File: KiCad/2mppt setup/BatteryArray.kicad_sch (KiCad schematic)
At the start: 4 parts

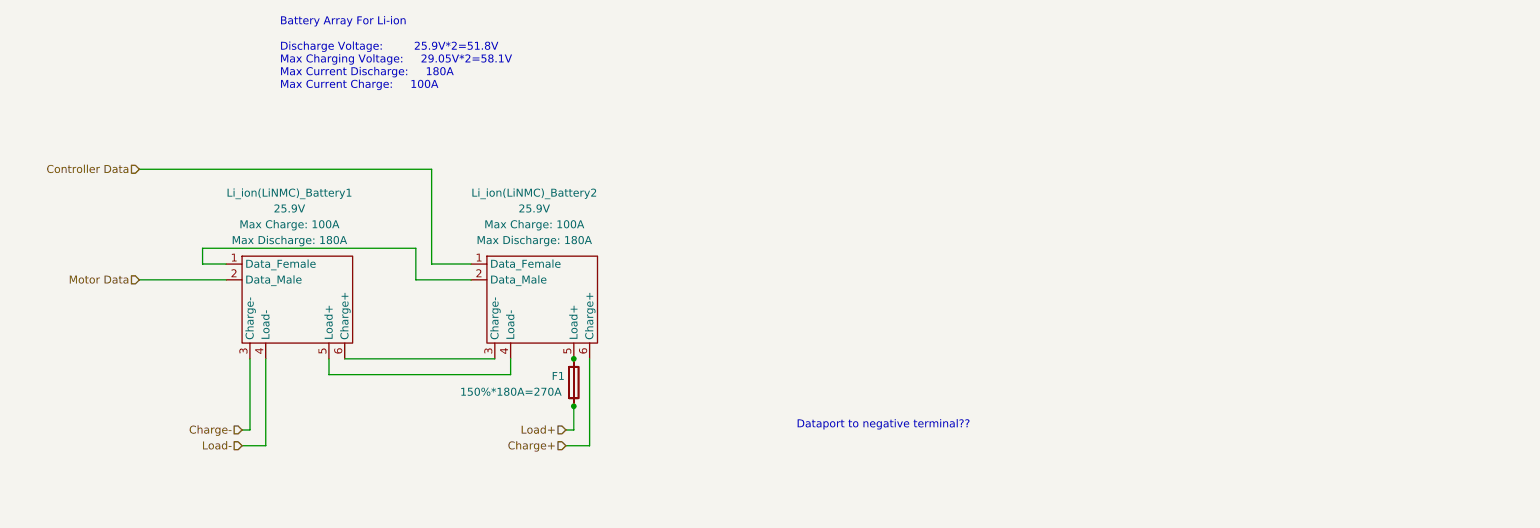
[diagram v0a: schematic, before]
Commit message: Fix wiring check issue
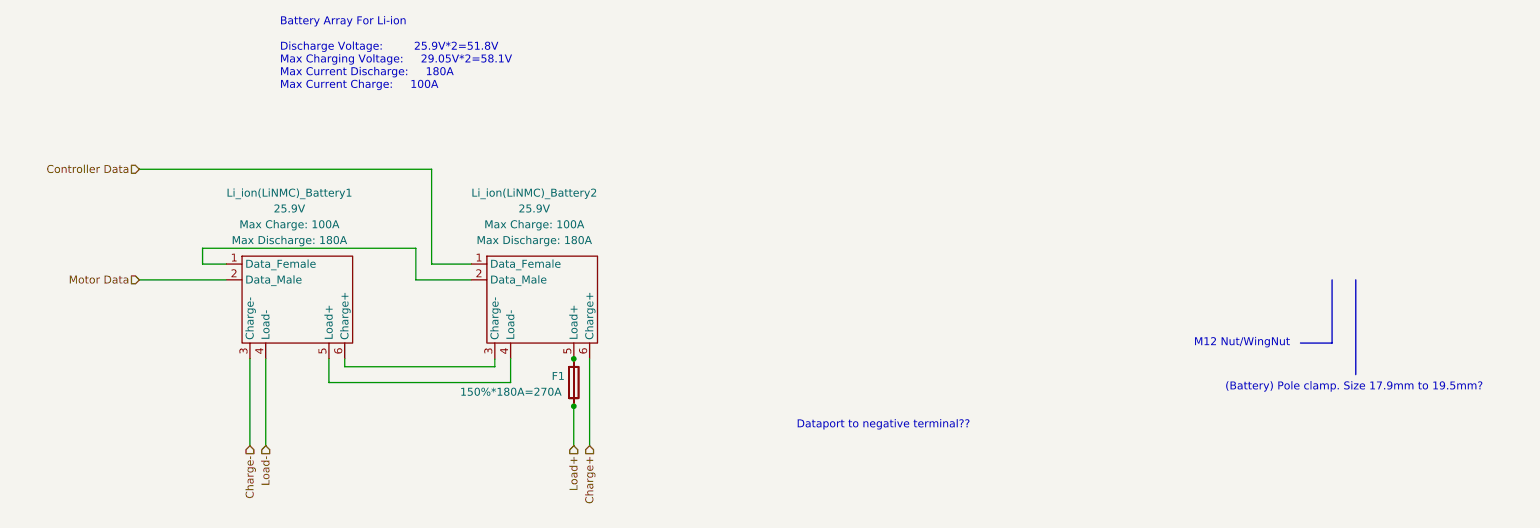
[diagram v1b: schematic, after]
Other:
- note added: "(Battery) Pole clamp. Size 17.9mm to 19.5mm?"
- note added: "M12 Nut/WingNut"

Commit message: KiCad_Skip & Schemdraw test
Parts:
- renumbered 150%*180A=270A_1 to 150%*180A=270A_2, F1 to F2, Li_ion(LiNMC)_Battery1 to Li_ion(LiNMC)_Battery3, Li_ion(LiNMC)_Battery2 to Li_ion(LiNMC)_Battery4
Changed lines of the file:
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@@
 	(text "Battery Array For Li-ion\n\nDischarge Voltage:	 	25.9V*2=51.8V\nMax Charging Voltage: 	29.05V*2=58.1V \nMax Current Discharge: 	180A\nMax Current Charge: 	100A"
 		(exclude_from_sim yes)
-		(at 86.106 25.908 0)
+		(at 85.852 34.29 0)
 		(effects
 			(font
@@
 		(dnp no)
 		(fields_autoplaced yes)
-		(property "Reference" "Li_ion(LiNMC)_Battery2"
+		(property "Reference" "Li_ion(LiNMC)_Battery4"
 			(at 127 48.26 0)
 			(effects
@@
 		(instances
 			(project "2mppt setup"
+				(path "/a5748c52-e651-4363-96d3-c9fc6357a5ef/3557b8e6-13fd-4121-8a05-5ebfb3204dff"
+					(reference "Li_ion(LiNMC)_Battery4")
+					(unit 1)
+				)
 				(path "/a5748c52-e651-4363-96d3-c9fc6357a5ef/5c90004e-845d-4999-8ab5-0ca9dd600da9"
 					(reference "Li_ion(LiNMC)_Battery2")
@@
 		(on_board yes)
 		(dnp no)
-		(property "Reference" "150%*180A=270A_1"
+		(property "Reference" "150%*180A=270A_2"
 			(at 113.538 79.502 0)
 			(effects
@@
 		)
 		(instances
-			(project ""
+			(project "2mppt setup"
+				(path "/a5748c52-e651-4363-96d3-c9fc6357a5ef/3557b8e6-13fd-4121-8a05-5ebfb3204dff"
+					(reference "150%*180A=270A_2")
+					(unit 1)
+				)
 				(path "/a5748c52-e651-4363-96d3-c9fc6357a5ef/5c90004e-845d-4999-8ab5-0ca9dd600da9"
 					(reference "150%*180A=270A_1")
@@
 		(dnp no)
 		(fields_autoplaced yes)
-		(property "Reference" "Li_ion(LiNMC)_Battery1"
+		(property "Reference" "Li_ion(LiNMC)_Battery3"
 			(at 87.63 48.26 0)
 			(effects
@@
 		)
 		(instances
-			(project ""
+			(project "2mppt setup"
+				(path "/a5748c52-e651-4363-96d3-c9fc6357a5ef/3557b8e6-13fd-4121-8a05-5ebfb3204dff"
+					(reference "Li_ion(LiNMC)_Battery3")
+					(unit 1)
+				)
 				(path "/a5748c52-e651-4363-96d3-c9fc6357a5ef/5c90004e-845d-4999-8ab5-0ca9dd600da9"
 					(reference "Li_ion(LiNMC)_Battery1")
@@
 		(on_board yes)
 		(dnp no)
-		(property "Reference" "F1"
+		(property "Reference" "F2"
 			(at 129.794 77.724 0)
 			(effects
@@
 		)
 		(instances
-			(project ""
+			(project "2mppt setup"
+				(path "/a5748c52-e651-4363-96d3-c9fc6357a5ef/3557b8e6-13fd-4121-8a05-5ebfb3204dff"
+					(reference "F2")
+					(unit 1)
+				)
 				(path "/a5748c52-e651-4363-96d3-c9fc6357a5ef/5c90004e-845d-4999-8ab5-0ca9dd600da9"
 					(reference "F1")
